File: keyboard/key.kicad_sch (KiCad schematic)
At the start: 2 parts, among them SW10 MX

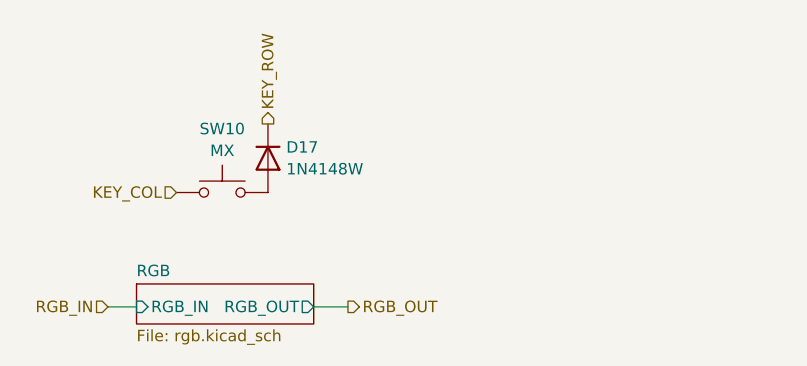
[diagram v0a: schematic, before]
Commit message: Minor keyboard schematics adjustments
No impact on the PCB
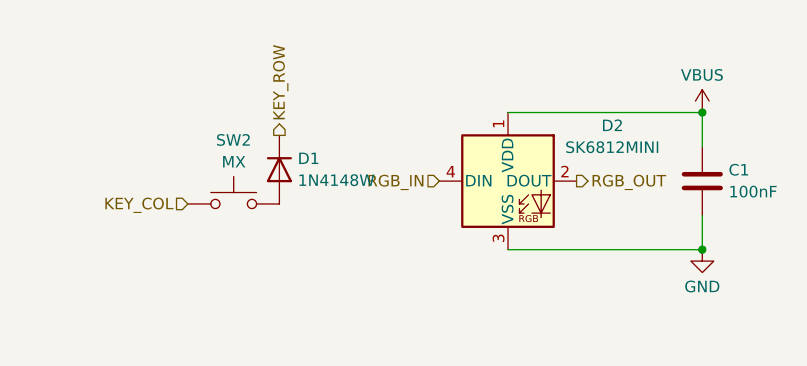
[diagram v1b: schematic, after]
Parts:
- removed D17: 1N4148W, Diode_SMD:D_SOD-123, symbol Device:D
- removed SW10: MX, Library:Kailh_socket_MX_1-00U, symbol Switch:SW_Push
- added C1: 100nF, Capacitor_SMD:C_0402_1005Metric, symbol Device:C
- added D1: 1N4148W, Diode_SMD:D_SOD-123, symbol Device:D
- added D2: SK6812MINI, LED_SMD:LED_SK6812MINI-E_3.2x2.8mm_P1.5mm_ReverseMount, symbol DecentUSB_Library:SK6812MINI
- added SW2: MX, Library:SMD_KEYBOARD-SW, symbol Switch:SW_Push
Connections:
- net KEY_COL: now also SW2.1
- net KEY_ROW: now also D1.1 (K)
- net RGB_IN: now also D2.4 (DIN)
- net RGB_OUT: now also D2.2 (DOUT)
- new net: D1.2 (A), SW2.2
- new net GND: C1.2, D2.3 (VSS)
- new net VBUS: C1.1, D2.1 (VDD)
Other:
- removed sheet RGB
